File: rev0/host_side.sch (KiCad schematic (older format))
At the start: 8 parts

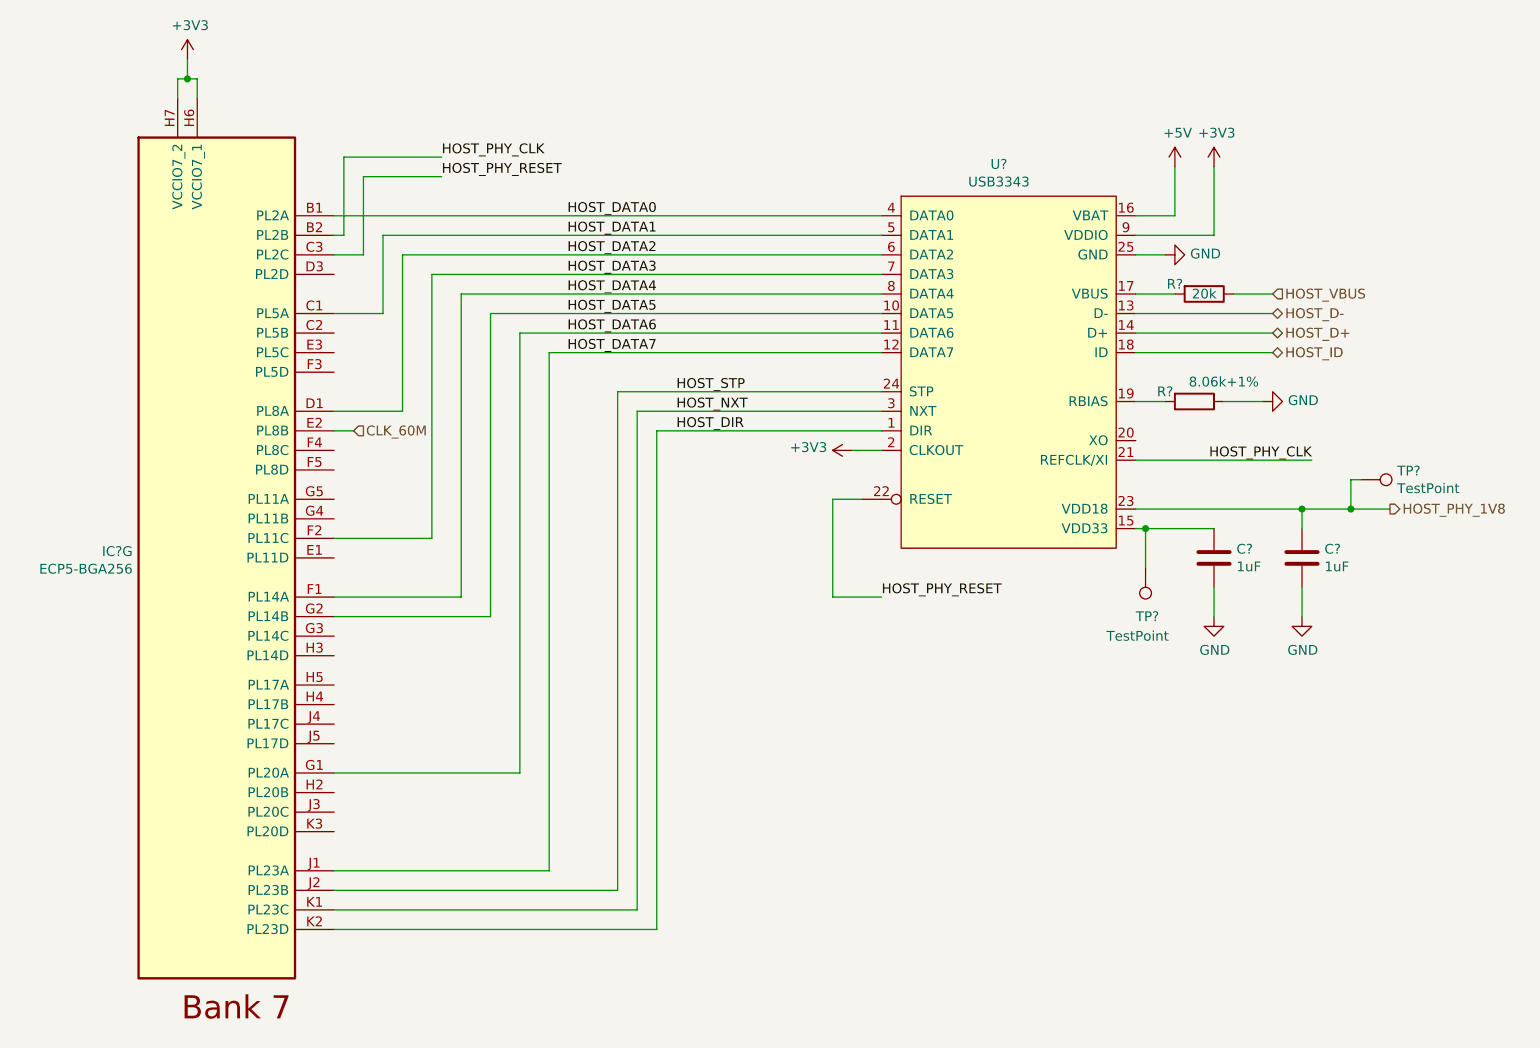
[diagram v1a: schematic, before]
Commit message: schematic: finish initial capture
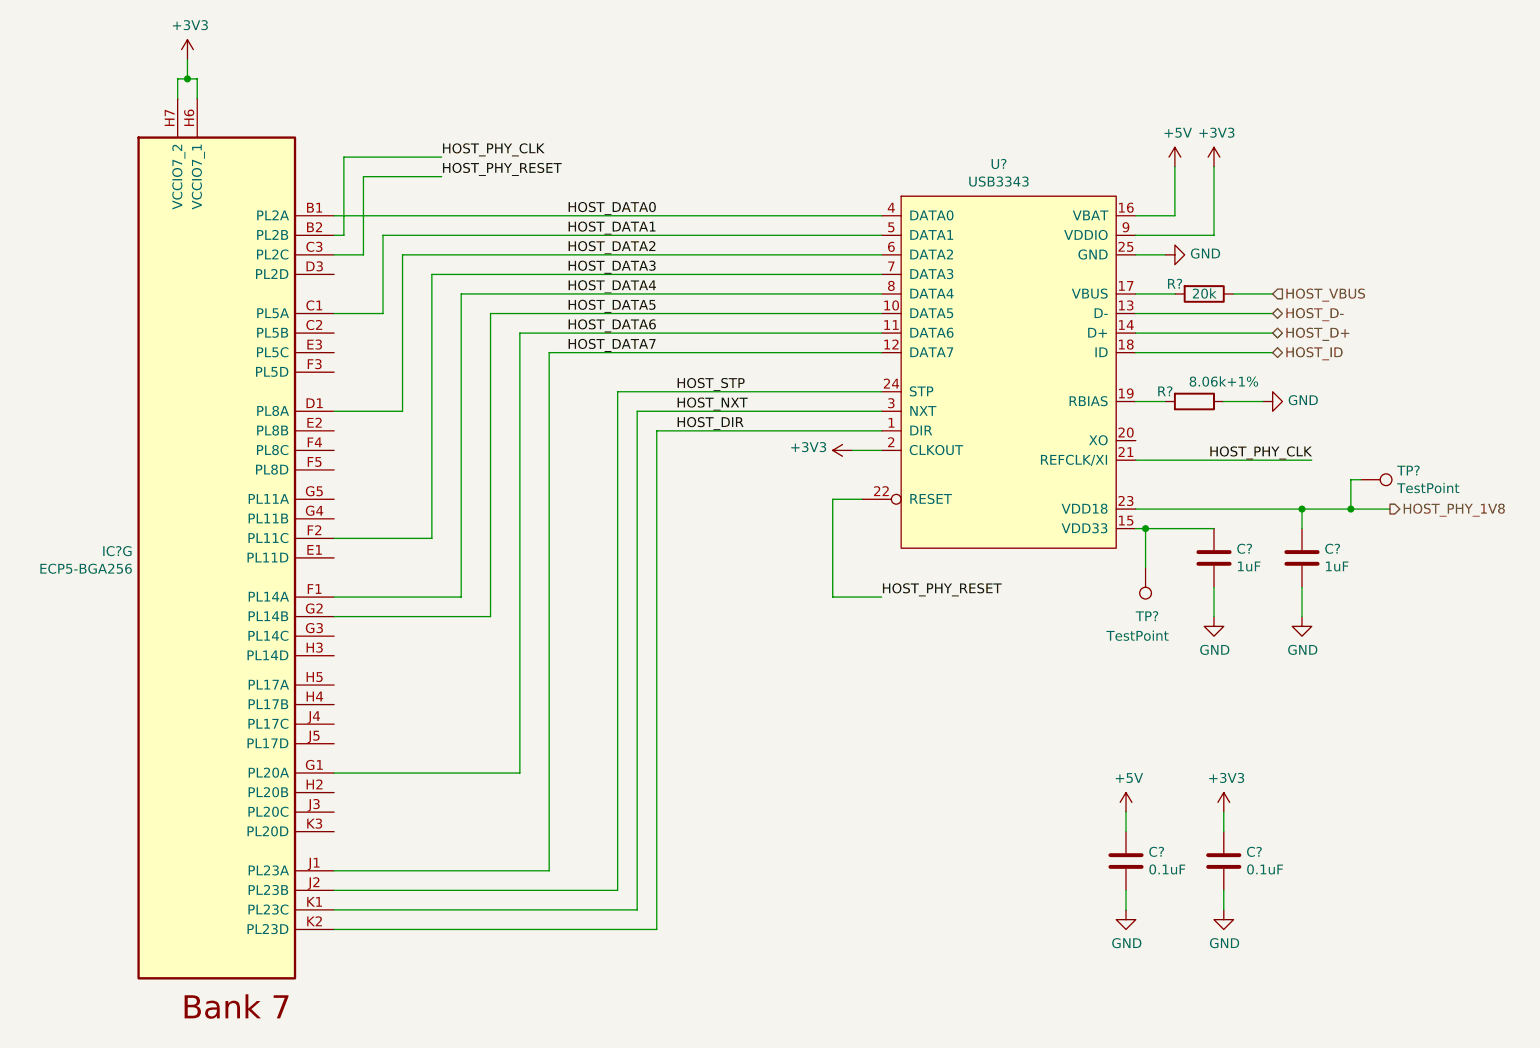
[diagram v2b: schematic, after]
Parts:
- added C? (x2): 0.1uF, symbol Device:C
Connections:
- net +3V3: now also C?.1
- net +5V: now also C?.1
- net GND: now also C?.2, C?.2
- net CLK_60M: no longer names the net of IC?.E2 (PL8B)
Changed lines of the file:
@@
 $Descr A4 11693 8268
 encoding utf-8
-Sheet 5 6
-Title ""
-Date ""
-Rev ""
-Comp ""
-Comment1 ""
+Sheet 9 9
+Title "LUNA: Upstream \"Host\" Section"
+Date "2019-10-20"
+Rev "r0"
+Comp "Great Scott Gadgets"
+Comment1 "Katherine J. Temkin"
 Comment2 ""
-Comment3 ""
+Comment3 "Licensed under the CERN OHL v1.2"
 Comment4 ""
 $EndDescr
@@
 	1    0    0    -1
 $EndComp
-Wire Wire Line
-	2700 3000 2800 3000
-Text HLabel 2800 3000 2    50   Input ~ 0
-CLK_60M
+$Comp
+L Device:C C?
+U 1 1 5DEDB896
+P 6750 5200
+AR Path="/5DCD9772/5DEDB896" Ref="C?"  Part="1"
+AR Path="/5DD754D4/5DEDB896" Ref="C?"  Part="1"
+F 0 "C?" H 6865 5245 50  0000 L CNN
+F 1 "0.1uF" H 6865 5155 50  0000 L CNN
+F 2 "" H 6788 5050 50  0001 C CNN
+F 3 "~" H 6750 5200 50  0001 C CNN
+	1    6750 5200
+	1    0    0    -1
+$EndComp
+$Comp
+L Device:C C?
+U 1 1 5DEDB89C
+P 7250 5200
+AR Path="/5DCD9772/5DEDB89C" Ref="C?"  Part="1"
+AR Path="/5DD754D4/5DEDB89C" Ref="C?"  Part="1"
+F 0 "C?" H 7365 5245 50  0000 L CNN
+F 1 "0.1uF" H 7365 5155 50  0000 L CNN
+F 2 "" H 7288 5050 50  0001 C CNN
+F 3 "~" H 7250 5200 50  0001 C CNN
+	1    7250 5200
+	1    0    0    -1
+$EndComp
+$Comp
+L power:+5V #PWR?
+U 1 1 5DEDB8A2
+P 6750 4950
+AR Path="/5DCD9772/5DEDB8A2" Ref="#PWR?"  Part="1"
+AR Path="/5DD754D4/5DEDB8A2" Ref="#PWR?"  Part="1"
+F 0 "#PWR?" H 6750 4800 50  0001 C CNN
+F 1 "+5V" H 6764 5123 50  0000 C CNN
+F 2 "" H 6750 4950 50  0001 C CNN
+F 3 "" H 6750 4950 50  0001 C CNN
+	1    6750 4950
+	1    0    0    -1
+$EndComp
+$Comp
+L power:+3V3 #PWR?
+U 1 1 5DEDB8A8
+P 7250 4950
+AR Path="/5DCD9772/5DEDB8A8" Ref="#PWR?"  Part="1"
+AR Path="/5DD754D4/5DEDB8A8" Ref="#PWR?"  Part="1"
+F 0 "#PWR?" H 7250 4800 50  0001 C CNN
+F 1 "+3V3" H 7264 5123 50  0000 C CNN
+F 2 "" H 7250 4950 50  0001 C CNN
+F 3 "" H 7250 4950 50  0001 C CNN
+	1    7250 4950
+	1    0    0    -1
+$EndComp
+$Comp
+L power:GND #PWR?
+U 1 1 5DEDB8AE
+P 6750 5450
+AR Path="/5DCD9772/5DEDB8AE" Ref="#PWR?"  Part="1"
+AR Path="/5DD754D4/5DEDB8AE" Ref="#PWR?"  Part="1"
+F 0 "#PWR?" H 6750 5200 50  0001 C CNN
+F 1 "GND" H 6754 5278 50  0000 C CNN
+F 2 "" H 6750 5450 50  0001 C CNN
+F 3 "" H 6750 5450 50  0001 C CNN
+	1    6750 5450
+	1    0    0    -1
+$EndComp
+$Comp
+L power:GND #PWR?
+U 1 1 5DEDB8B4
+P 7250 5450
+AR Path="/5DCD9772/5DEDB8B4" Ref="#PWR?"  Part="1"
+AR Path="/5DD754D4/5DEDB8B4" Ref="#PWR?"  Part="1"
+F 0 "#PWR?" H 7250 5200 50  0001 C CNN
+F 1 "GND" H 7254 5278 50  0000 C CNN
+F 2 "" H 7250 5450 50  0001 C CNN
+F 3 "" H 7250 5450 50  0001 C CNN
+	1    7250 5450
+	1    0    0    -1
+$EndComp
+Wire Wire Line
+	7250 4950 7250 5050
+Wire Wire Line
+	6750 4950 6750 5050
+Wire Wire Line
+	6750 5350 6750 5450
+Wire Wire Line
+	7250 5350 7250 5450
 $EndSCHEMATC

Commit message: rev0: finish capture and start routing (woo!)
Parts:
- added R24: 10K, Resistor_SMD:R_0402_1005Metric, symbol Device:R
- C47, C49: renamed from C?; footprint (none) -> Capacitor_SMD:C_0402_1005Metric
- C48, C50: renamed from C?; footprint (none) -> Capacitor_SMD:C_0603_1608Metric
- IC1: renamed from IC?; footprint BGA256C80P16X16_1400X1400X170 -> luna:lattice_cabga256
- R20, R21: renamed from R?; footprint (none) -> Resistor_SMD:R_0402_1005Metric
- TP10, TP9: renamed from TP?; footprint (none) -> TestPoint:TestPoint_Pad_1.0x1.0mm
- U11: renamed from U?; footprint (none) -> Package_DFN_QFN:VQFN-24-1EP_4x4mm_P0.5mm_EP2.45x2.45mm
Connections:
- net +3V3: now also R24.2
- net HOST_PHY_RESET: now also R24.1
- no-connect marks 0 -> 20
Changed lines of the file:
@@
 $Descr A4 11693 8268
 encoding utf-8
-Sheet 9 9
+Sheet 8 9
 Title "LUNA: Upstream \"Host\" Section"
 Date "2019-10-20"
@@
 $EndDescr
 $Comp
-L fpgas_and_processors:ECP5-BGA256 IC?
+L fpgas_and_processors:ECP5-BGA256 IC1
 U 7 1 5DD79283
 P 1700 1500
-F 0 "IC?" H 1670 -617 50  0000 R CNN
+F 0 "IC1" H 1670 -617 50  0000 R CNN
 F 1 "ECP5-BGA256" H 1670 -707 50  0000 R CNN
-F 2 "BGA256C80P16X16_1400X1400X170" H -1500 4950 50  0001 L CNN
+F 2 "luna:lattice_cabga256" H -1500 4950 50  0001 L CNN
 F 3 "" H -1950 5900 50  0001 L CNN
 F 4 "FPGA - Field Programmable Gate Array ECP5; 12k LUTs; 1.1V" H -1950 5800 50  0001 L CNN "Description"
@@
 	4350 5550 4350 3000
 $Comp
-L power:+3V3 #PWR?
+L power:+3V3 #PWR088
 U 1 1 5DD90047
 P 5350 3100
-F 0 "#PWR?" H 5350 2950 50  0001 C CNN
+F 0 "#PWR088" H 5350 2950 50  0001 C CNN
 F 1 "+3V3" V 5365 3228 50  0000 L CNN
 F 2 "" H 5350 3100 50  0001 C CNN
@@
 P 7150 2300
 AR Path="/5DCD9772/5DD9AF21" Ref="R?"  Part="1"
-AR Path="/5DD754D4/5DD9AF21" Ref="R?"  Part="1"
-F 0 "R?" V 7100 2150 50  0000 C CNN
+AR Path="/5DD754D4/5DD9AF21" Ref="R21"  Part="1"
+F 0 "R21" V 7100 2050 50  0000 C CNN
 F 1 "20k" V 7150 2300 50  0000 C CNN
-F 2 "" V 7080 2300 50  0001 C CNN
+F 2 "Resistor_SMD:R_0402_1005Metric" V 7080 2300 50  0001 C CNN
 F 3 "~" H 7150 2300 50  0001 C CNN
 	1    7150 2300
@@
 P 7450 2850
 AR Path="/5DCD9772/5DD9AF1A" Ref="#PWR?"  Part="1"
-AR Path="/5DD754D4/5DD9AF1A" Ref="#PWR?"  Part="1"
-F 0 "#PWR?" H 7450 2600 50  0001 C CNN
+AR Path="/5DD754D4/5DD9AF1A" Ref="#PWR097"  Part="1"
+F 0 "#PWR097" H 7450 2600 50  0001 C CNN
 F 1 "GND" V 7455 2722 50  0000 R CNN
 F 2 "" H 7450 2850 50  0001 C CNN
@@
 P 7100 2850
 AR Path="/5DCD9772/5DD9AF13" Ref="R?"  Part="1"
-AR Path="/5DD754D4/5DD9AF13" Ref="R?"  Part="1"
-F 0 "R?" V 7050 2700 50  0000 C CNN
+AR Path="/5DD754D4/5DD9AF13" Ref="R20"  Part="1"
+F 0 "R20" V 7050 2650 50  0000 C CNN
 F 1 "8.06k+1%" V 7000 3000 50  0000 C CNN
-F 2 "" V 7030 2850 50  0001 C CNN
+F 2 "Resistor_SMD:R_0402_1005Metric" V 7030 2850 50  0001 C CNN
 F 3 "~" H 7100 2850 50  0001 C CNN
 	1    7100 2850
@@
 P 7200 1650
 AR Path="/5DCD9772/5DD9AF0B" Ref="#PWR?"  Part="1"
-AR Path="/5DD754D4/5DD9AF0B" Ref="#PWR?"  Part="1"
-F 0 "#PWR?" H 7200 1500 50  0001 C CNN
+AR Path="/5DD754D4/5DD9AF0B" Ref="#PWR093"  Part="1"
+F 0 "#PWR093" H 7200 1500 50  0001 C CNN
 F 1 "+3V3" H 7214 1823 50  0000 C CNN
 F 2 "" H 7200 1650 50  0001 C CNN
@@
 P 7000 1650
 AR Path="/5DCD9772/5DD9AF05" Ref="#PWR?"  Part="1"
-AR Path="/5DD754D4/5DD9AF05" Ref="#PWR?"  Part="1"
-F 0 "#PWR?" H 7000 1500 50  0001 C CNN
+AR Path="/5DD754D4/5DD9AF05" Ref="#PWR092"  Part="1"
+F 0 "#PWR092" H 7000 1500 50  0001 C CNN
 F 1 "+5V" H 7014 1823 50  0000 C CNN
 F 2 "" H 7000 1650 50  0001 C CNN
@@
 P 6950 2100
 AR Path="/5DCD9772/5DD9AEFD" Ref="#PWR?"  Part="1"
-AR Path="/5DD754D4/5DD9AEFD" Ref="#PWR?"  Part="1"
-F 0 "#PWR?" H 6950 1850 50  0001 C CNN
+AR Path="/5DD754D4/5DD9AEFD" Ref="#PWR091"  Part="1"
+F 0 "#PWR091" H 6950 1850 50  0001 C CNN
 F 1 "GND" V 6955 1972 50  0000 R CNN
 F 2 "" H 6950 2100 50  0001 C CNN
@@
 P 6850 3700
 AR Path="/5DCD9772/5DD9AEEC" Ref="TP?"  Part="1"
-AR Path="/5DD754D4/5DD9AEEC" Ref="TP?"  Part="1"
-F 0 "TP?" H 6900 3950 50  0000 R CNN
+AR Path="/5DD754D4/5DD9AEEC" Ref="TP9"  Part="1"
+F 0 "TP9" H 6900 3950 50  0000 R CNN
 F 1 "TestPoint" H 7050 4050 50  0000 R CNN
-F 2 "" H 7050 3700 50  0001 C CNN
+F 2 "TestPoint:TestPoint_Pad_1.0x1.0mm" H 7050 3700 50  0001 C CNN
 F 3 "~" H 7050 3700 50  0001 C CNN
 	1    6850 3700
@@
 P 7950 3250
 AR Path="/5DCD9772/5DD9AEE2" Ref="TP?"  Part="1"
-AR Path="/5DD754D4/5DD9AEE2" Ref="TP?"  Part="1"
-F 0 "TP?" V 7905 3437 50  0000 L CNN
+AR Path="/5DD754D4/5DD9AEE2" Ref="TP10"  Part="1"
+F 0 "TP10" V 7905 3437 50  0000 L CNN
 F 1 "TestPoint" V 7995 3437 50  0000 L CNN
-F 2 "" H 8150 3250 50  0001 C CNN
+F 2 "TestPoint:TestPoint_Pad_1.0x1.0mm" H 8150 3250 50  0001 C CNN
 F 3 "~" H 8150 3250 50  0001 C CNN
 	1    7950 3250
@@
 P 7650 3950
 AR Path="/5DCD9772/5DD9AED7" Ref="#PWR?"  Part="1"
-AR Path="/5DD754D4/5DD9AED7" Ref="#PWR?"  Part="1"
-F 0 "#PWR?" H 7650 3700 50  0001 C CNN
+AR Path="/5DD754D4/5DD9AED7" Ref="#PWR098"  Part="1"
+F 0 "#PWR098" H 7650 3700 50  0001 C CNN
 F 1 "GND" H 7654 3778 50  0000 C CNN
 F 2 "" H 7650 3950 50  0001 C CNN
@@
 P 7650 3650
 AR Path="/5DCD9772/5DD9AED1" Ref="C?"  Part="1"
-AR Path="/5DD754D4/5DD9AED1" Ref="C?"  Part="1"
-F 0 "C?" H 7765 3695 50  0000 L CNN
+AR Path="/5DD754D4/5DD9AED1" Ref="C50"  Part="1"
+F 0 "C50" H 7765 3695 50  0000 L CNN
 F 1 "1uF" H 7765 3605 50  0000 L CNN
-F 2 "" H 7688 3500 50  0001 C CNN
+F 2 "Capacitor_SMD:C_0603_1608Metric" H 7688 3500 50  0001 C CNN
 F 3 "~" H 7650 3650 50  0001 C CNN
 	1    7650 3650
@@
 P 7200 3950
 AR Path="/5DCD9772/5DD9AEC9" Ref="#PWR?"  Part="1"
-AR Path="/5DD754D4/5DD9AEC9" Ref="#PWR?"  Part="1"
-F 0 "#PWR?" H 7200 3700 50  0001 C CNN
+AR Path="/5DD754D4/5DD9AEC9" Ref="#PWR094"  Part="1"
+F 0 "#PWR094" H 7200 3700 50  0001 C CNN
 F 1 "GND" H 7204 3778 50  0000 C CNN
 F 2 "" H 7200 3950 50  0001 C CNN
@@
 P 7200 3650
 AR Path="/5DCD9772/5DD9AEC3" Ref="C?"  Part="1"
-AR Path="/5DD754D4/5DD9AEC3" Ref="C?"  Part="1"
-F 0 "C?" H 7315 3695 50  0000 L CNN
+AR Path="/5DD754D4/5DD9AEC3" Ref="C48"  Part="1"
+F 0 "C48" H 7315 3695 50  0000 L CNN
 F 1 "1uF" H 7315 3605 50  0000 L CNN
-F 2 "" H 7238 3500 50  0001 C CNN
+F 2 "Capacitor_SMD:C_0603_1608Metric" H 7238 3500 50  0001 C CNN
 F 3 "~" H 7200 3650 50  0001 C CNN
 	1    7200 3650
@@
 P 5500 1800
 AR Path="/5DCD9772/5DD9AEA4" Ref="U?"  Part="1"
-AR Path="/5DD754D4/5DD9AEA4" Ref="U?"  Part="1"
-F 0 "U?" H 6100 1963 50  0000 C CNN
+AR Path="/5DD754D4/5DD9AEA4" Ref="U11"  Part="1"
+F 0 "U11" H 6100 1963 50  0000 C CNN
 F 1 "USB3343" H 6100 1873 50  0000 C CNN
-F 2 "" H 5500 1800 50  0001 C CNN
+F 2 "Package_DFN_QFN:VQFN-24-1EP_4x4mm_P0.5mm_EP2.45x2.45mm" H 5500 1800 50  0001 C CNN
 F 3 "http://ww1.microchip.com/downloads/en/DeviceDoc/334x.pdf" H 5500 1800 50  0001 C CNN
 	1    5500 1800
@@
 	1950 1200 2000 1200
 $Comp
-L power:+3V3 #PWR?
+L power:+3V3 #PWR087
 U 1 1 5DDBCF19
 P 1950 1100
-F 0 "#PWR?" H 1950 950 50  0001 C CNN
+F 0 "#PWR087" H 1950 950 50  0001 C CNN
 F 1 "+3V3" H 1964 1273 50  0000 C CNN
 F 2 "" H 1950 1100 50  0001 C CNN
@@
 P 6750 5200
 AR Path="/5DCD9772/5DEDB896" Ref="C?"  Part="1"
-AR Path="/5DD754D4/5DEDB896" Ref="C?"  Part="1"
-F 0 "C?" H 6865 5245 50  0000 L CNN
+AR Path="/5DD754D4/5DEDB896" Ref="C47"  Part="1"
+F 0 "C47" H 6865 5245 50  0000 L CNN
 F 1 "0.1uF" H 6865 5155 50  0000 L CNN
-F 2 "" H 6788 5050 50  0001 C CNN
+F 2 "Capacitor_SMD:C_0402_1005Metric" H 6788 5050 50  0001 C CNN
 F 3 "~" H 6750 5200 50  0001 C CNN
 	1    6750 5200
@@
 P 7250 5200
 AR Path="/5DCD9772/5DEDB89C" Ref="C?"  Part="1"
-AR Path="/5DD754D4/5DEDB89C" Ref="C?"  Part="1"
-F 0 "C?" H 7365 5245 50  0000 L CNN
+AR Path="/5DD754D4/5DEDB89C" Ref="C49"  Part="1"
+F 0 "C49" H 7365 5245 50  0000 L CNN
 F 1 "0.1uF" H 7365 5155 50  0000 L CNN
-F 2 "" H 7288 5050 50  0001 C CNN
+F 2 "Capacitor_SMD:C_0402_1005Metric" H 7288 5050 50  0001 C CNN
 F 3 "~" H 7250 5200 50  0001 C CNN
 	1    7250 5200
@@
 P 6750 4950
 AR Path="/5DCD9772/5DEDB8A2" Ref="#PWR?"  Part="1"
-AR Path="/5DD754D4/5DEDB8A2" Ref="#PWR?"  Part="1"
-F 0 "#PWR?" H 6750 4800 50  0001 C CNN
+AR Path="/5DD754D4/5DEDB8A2" Ref="#PWR089"  Part="1"
+F 0 "#PWR089" H 6750 4800 50  0001 C CNN
 F 1 "+5V" H 6764 5123 50  0000 C CNN
 F 2 "" H 6750 4950 50  0001 C CNN
@@
 P 7250 4950
 AR Path="/5DCD9772/5DEDB8A8" Ref="#PWR?"  Part="1"
-AR Path="/5DD754D4/5DEDB8A8" Ref="#PWR?"  Part="1"
-F 0 "#PWR?" H 7250 4800 50  0001 C CNN
+AR Path="/5DD754D4/5DEDB8A8" Ref="#PWR095"  Part="1"
+F 0 "#PWR095" H 7250 4800 50  0001 C CNN
 F 1 "+3V3" H 7264 5123 50  0000 C CNN
 F 2 "" H 7250 4950 50  0001 C CNN
@@
 P 6750 5450
 AR Path="/5DCD9772/5DEDB8AE" Ref="#PWR?"  Part="1"
-AR Path="/5DD754D4/5DEDB8AE" Ref="#PWR?"  Part="1"
-F 0 "#PWR?" H 6750 5200 50  0001 C CNN
+AR Path="/5DD754D4/5DEDB8AE" Ref="#PWR090"  Part="1"
+F 0 "#PWR090" H 6750 5200 50  0001 C CNN
 F 1 "GND" H 6754 5278 50  0000 C CNN
 F 2 "" H 6750 5450 50  0001 C CNN
@@
 P 7250 5450
 AR Path="/5DCD9772/5DEDB8B4" Ref="#PWR?"  Part="1"
-AR Path="/5DD754D4/5DEDB8B4" Ref="#PWR?"  Part="1"
-F 0 "#PWR?" H 7250 5200 50  0001 C CNN
+AR Path="/5DD754D4/5DEDB8B4" Ref="#PWR096"  Part="1"
+F 0 "#PWR096" H 7250 5200 50  0001 C CNN
 F 1 "GND" H 7254 5278 50  0000 C CNN
 F 2 "" H 7250 5450 50  0001 C CNN
@@
 Wire Wire Line
 	7250 5350 7250 5450
+$Comp
+L Device:R R24
+U 1 1 5E14D51C
+P 5000 3350
+F 0 "R24" V 5100 3350 50  0000 C CNN
+F 1 "10K" V 5000 3350 50  0000 C CNN
+F 2 "Resistor_SMD:R_0402_1005Metric" V 4930 3350 50  0001 C CNN
+F 3 "~" H 5000 3350 50  0001 C CNN
+	1    5000 3350
+	0    1    1    0
+$EndComp
+Wire Wire Line
+	5150 3350 5250 3350
+Connection ~ 5250 3350
+Wire Wire Line
+	4850 3350 4750 3350
+$Comp
+L ibp-hyperram-cache:+3.3V #PWR0101
+U 1 1 5E151861
+P 4750 3350
+F 0 "#PWR0101" H 4750 3200 50  0001 C CNN
+F 1 "+3.3V" V 4765 3478 50  0000 L CNN
+F 2 "" H 4750 3350 50  0001 C CNN
+F 3 "" H 4750 3350 50  0001 C CNN
+	1    4750 3350
+	0    -1   -1   0
+$EndComp
+NoConn ~ 2700 2200
+NoConn ~ 2700 2500
+NoConn ~ 2700 2600
+NoConn ~ 2700 2700
+NoConn ~ 2700 3000
+NoConn ~ 2700 3100
+NoConn ~ 2700 3200
+NoConn ~ 2700 3350
+NoConn ~ 2700 3450
+NoConn ~ 2700 3650
+NoConn ~ 2700 4050
+NoConn ~ 2700 4150
+NoConn ~ 2700 4300
+NoConn ~ 2700 4400
+NoConn ~ 2700 4500
+NoConn ~ 2700 4600
+NoConn ~ 2700 4850
+NoConn ~ 2700 4950
+NoConn ~ 2700 5050
+NoConn ~ 6800 3050
 $EndSCHEMATC

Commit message: rev0: clean up library references and backup files
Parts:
- U11: symbol rhododendron:USB3343 -> usb:USB3343
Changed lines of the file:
@@
 EESchema Schematic File Version 4
 LIBS:luna_rev0-cache
-EELAYER 29 0
+EELAYER 30 0
 EELAYER END
 $Descr A4 11693 8268
@@
 	6800 3150 7700 3150
 $Comp
-L rhododendron:USB3343 U?
+L usb:USB3343 U?
 U 1 1 5DD9AEA4
 P 5500 1800
@@
 	5150 3350 5250 3350
 Connection ~ 5250 3350
-Wire Wire Line
-	4850 3350 4750 3350
-$Comp
-L ibp-hyperram-cache:+3.3V #PWR0101
-U 1 1 5E151861
-P 4750 3350
-F 0 "#PWR0101" H 4750 3200 50  0001 C CNN
-F 1 "+3.3V" V 4765 3478 50  0000 L CNN
-F 2 "" H 4750 3350 50  0001 C CNN
-F 3 "" H 4750 3350 50  0001 C CNN
-	1    4750 3350
-	0    -1   -1   0
-$EndComp
 NoConn ~ 2700 2200
 NoConn ~ 2700 2500
@@
 NoConn ~ 2700 5050
 NoConn ~ 6800 3050
+$Comp
+L power:+3V3 #PWR?
+U 1 1 5DD76B4C
+P 4750 3350
+F 0 "#PWR?" H 4750 3200 50  0001 C CNN
+F 1 "+3V3" V 4765 3478 50  0000 L CNN
+F 2 "" H 4750 3350 50  0001 C CNN
+F 3 "" H 4750 3350 50  0001 C CNN
+	1    4750 3350
+	0    -1   -1   0
+$EndComp
+Wire Wire Line
+	4750 3350 4850 3350
 $EndSCHEMATC

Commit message: rev0: more routing scaffolding
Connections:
- net HOST_DATA0: now also IC1.G2 (PL14B); no longer IC1.B1 (PL2A)
- net HOST_DATA1: now also IC1.G1 (PL20A); no longer IC1.C1 (PL5A)
- net HOST_DATA2: now also IC1.F2 (PL11C); no longer IC1.D1 (PL8A)
- net HOST_DATA3: now also IC1.F1 (PL14A); no longer IC1.F2 (PL11C)
- net HOST_DATA4: now also IC1.E1 (PL11D); no longer IC1.F1 (PL14A)
- net HOST_DATA5: now also IC1.D1 (PL8A); no longer IC1.G2 (PL14B)
- net HOST_DATA6: now also IC1.C1 (PL5A); no longer IC1.G1 (PL20A)
- net HOST_DATA7: now also IC1.B1 (PL2A); no longer IC1.J1 (PL23A)
- net HOST_DIR: now also IC1.J1 (PL23A); no longer IC1.K2 (PL23D)
- net HOST_NXT: now also IC1.H2 (PL20B); no longer IC1.K1 (PL23C)
- net HOST_PHY_CLK: now also IC1.K2 (PL23D); no longer IC1.B2 (PL2B)
- net HOST_PHY_RESET: now also IC1.K1 (PL23C); no longer IC1.C3 (PL2C)
- no-connect marks 20 -> 18
